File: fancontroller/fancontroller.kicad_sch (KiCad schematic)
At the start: 9 parts, among them SW1 SW_RESET, SW2 SW_BOOT, U1 ESP32-WROOM-32, U2 AMS1117-3.3

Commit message: KIcad messing
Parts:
- removed C1: 1uF, symbol Device:C
- removed C2, C4: 10uF, symbol Device:C
- removed C3: 0.1uF, symbol Device:C
- removed R1: 10k, symbol Device:R
- removed SW1: SW_RESET, symbol Switch:SW_Push
- removed SW2: SW_BOOT, symbol Switch:SW_Push
- removed U1: ESP32-WROOM-32, RF_Module:ESP32-WROOM-32, symbol RF_Module:ESP32-WROOM-32
- removed U2: AMS1117-3.3, Package_TO_SOT_SMD:SOT-223-3_TabPin2, symbol Regulator_Linear:AMS1117-3.3
- added C6: 10uF, Capacitor_THT:CP_Radial_D4.0mm_P1.50mm, symbol Device:C_Polarized
- added C7, C9: 0.1uF, Capacitor_THT:C_Disc_D3.0mm_W2.0mm_P2.50mm, symbol Device:C
- added C8: 100uF, Capacitor_THT:CP_Radial_D5.0mm_P2.00mm, symbol Device:C_Polarized
- added J2: Power Terminal, TerminalBlock:TerminalBlock_bornier-2_P5.08mm, symbol Connector:Screw_Terminal_01x02
- added J3: Programmer, Connector_PinHeader_2.54mm:PinHeader_1x04_P2.54mm_Vertical, symbol Connector:Conn_01x04_Male
- added J4: Relay board output, Connector_PinHeader_2.54mm:PinHeader_1x10_P2.54mm_Vertical, symbol Connector:Conn_01x10_Male
- added J5: I2C, Connector_PinHeader_2.54mm:PinHeader_1x04_P2.54mm_Vertical, symbol Connector:Conn_01x04_Male
- added R2, R3, R4, R5: 10k, Resistor_THT:R_Axial_DIN0207_L6.3mm_D2.5mm_P7.62mm_Horizontal, symbol Device:R
- added R6, R7, R8, R9: 470, Resistor_THT:R_Axial_DIN0207_L6.3mm_D2.5mm_P7.62mm_Horizontal, symbol Device:R
- added SW3: SW_Push, symbol Switch:SW_Push
- added U3: AMS1117-3.3, Package_TO_SOT_SMD:SOT-223-3_TabPin2, symbol Regulator_Linear:AMS1117-3.3
- added U4: ESP-12F, RF_Module:ESP-12E, symbol RF_Module:ESP-12F
- added U5: 74HC595, Package_DIP:DIP-16_W7.62mm_Socket, symbol 74xx:74HC595
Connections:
- net +3.3V: now also J3.1 (Pin_1)
- net GND: now also C6.2, C7.1, C8.2, C9.2, J2.2 (Pin_2), J3.4 (Pin_4), J4.1 (Pin_1), J5.4 (Pin_4), R5.1, SW3.1, U3.1 (GND), U4.15 (GND), U5.13 (~{OE}), U5.8 (GND)
- net RX: now also J3.2 (Pin_2), R7.2
- net TX: now also J3.3 (Pin_3), R6.1
- new net: J4.8 (Pin_8), U5.1 (QB)
- new net: J4.9 (Pin_9), U5.15 (QA)
- new net: J4.7 (Pin_7), U5.2 (QC)
- new net: J4.6 (Pin_6), U5.3 (QD)
- new net: J4.5 (Pin_5), U5.4 (QE)
- new net: J4.4 (Pin_4), U5.5 (QF)
- new net: J4.3 (Pin_3), U5.6 (QG)
- new net: J4.2 (Pin_2), U5.7 (QH)
- new net: R5.2, U4.16 (GPIO15)
- new net: R7.1, U4.21 (GPIO3/RXD)
- new net: R6.2, U4.22 (GPIO1/TXD)
- new net: C7.2, R4.1, U4.3 (EN)
- new net +3V3: C8.1, C9.1, J5.1 (Pin_1), R2.1, R3.1, R4.2, R8.1, R9.1, U3.2 (VO), U4.8 (VCC), U5.10 (~{SRCLR}), U5.16 (VCC)
- new net +5V: C6.1, J2.1 (Pin_1), J4.10 (Pin_10), U3.3 (VI)
- new net GPIO0: R2.2, SW3.2, U4.18 (GPIO0)
- new net MD_1: U4.6 (GPIO12), U5.12 (RCLK)
- new net MD_2: U4.7 (GPIO13), U5.11 (SRCLK)
- new net MD_3: U4.5 (GPIO14), U5.14 (SER)
- new net RST: R3.2, U4.1 (~{RST})
- new net SCL: J5.2 (Pin_2), R9.2, U4.20 (GPIO5)
- new net SDA: J5.3 (Pin_3), R8.2, U4.19 (GPIO4)
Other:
- note added: "Enabling booting"
- note added: "Output Multiplexer"
- note added: "Power circuit"

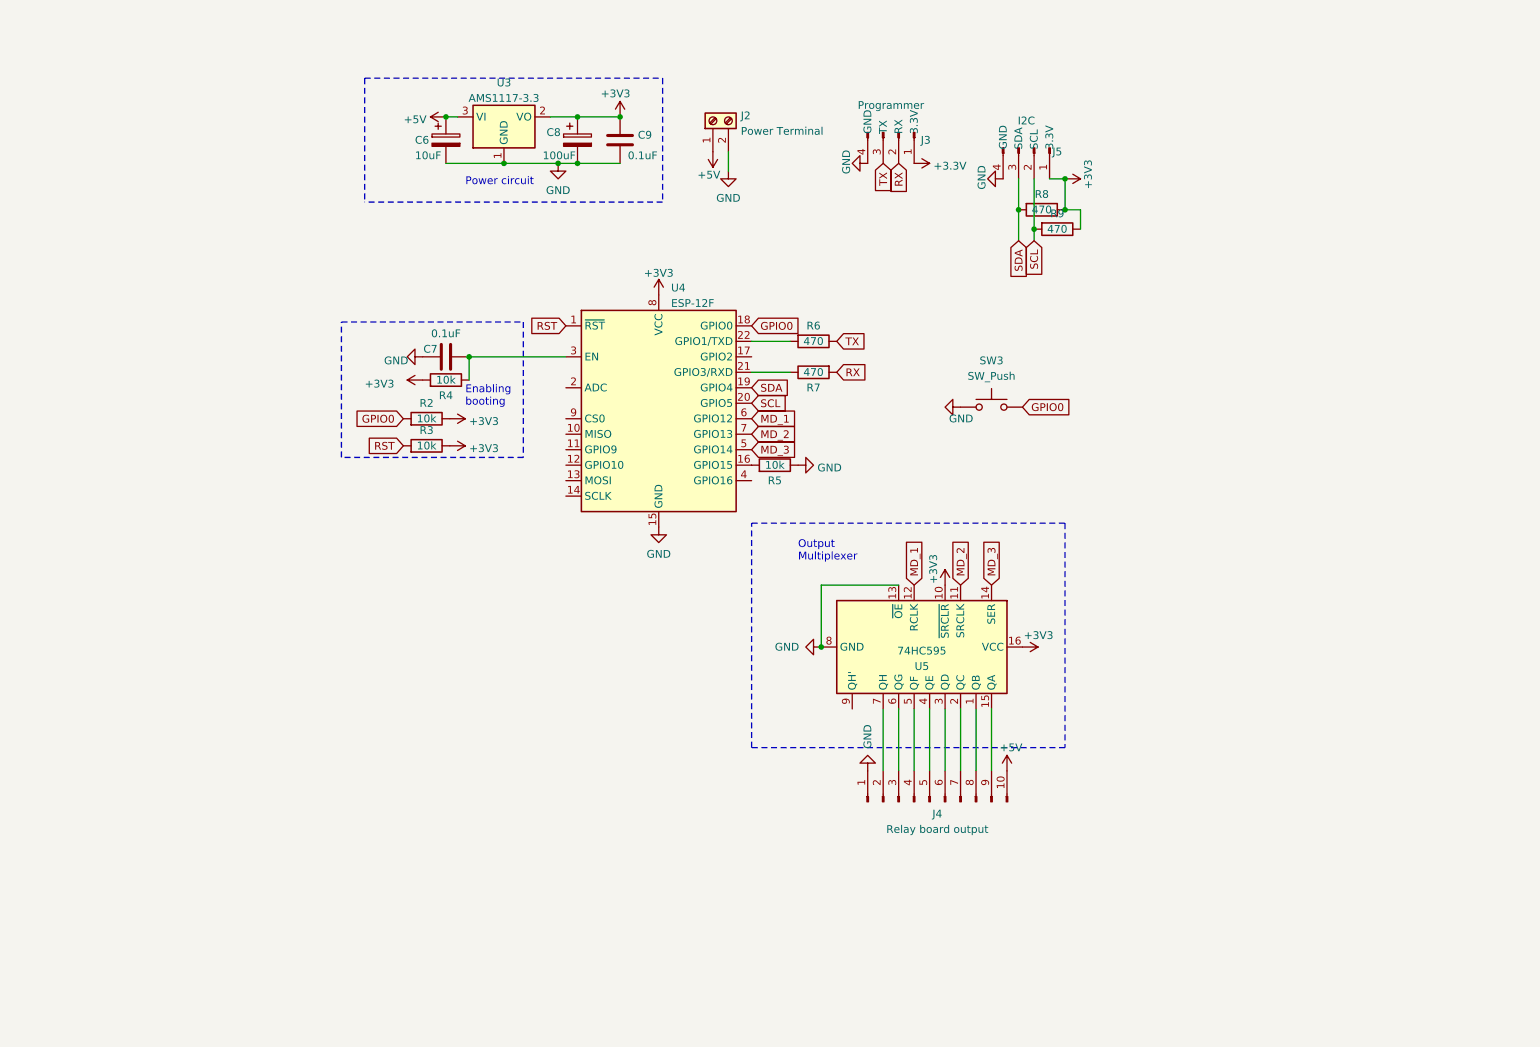
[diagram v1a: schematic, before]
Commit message: Auf esp32 festlegen und schematik anfangen
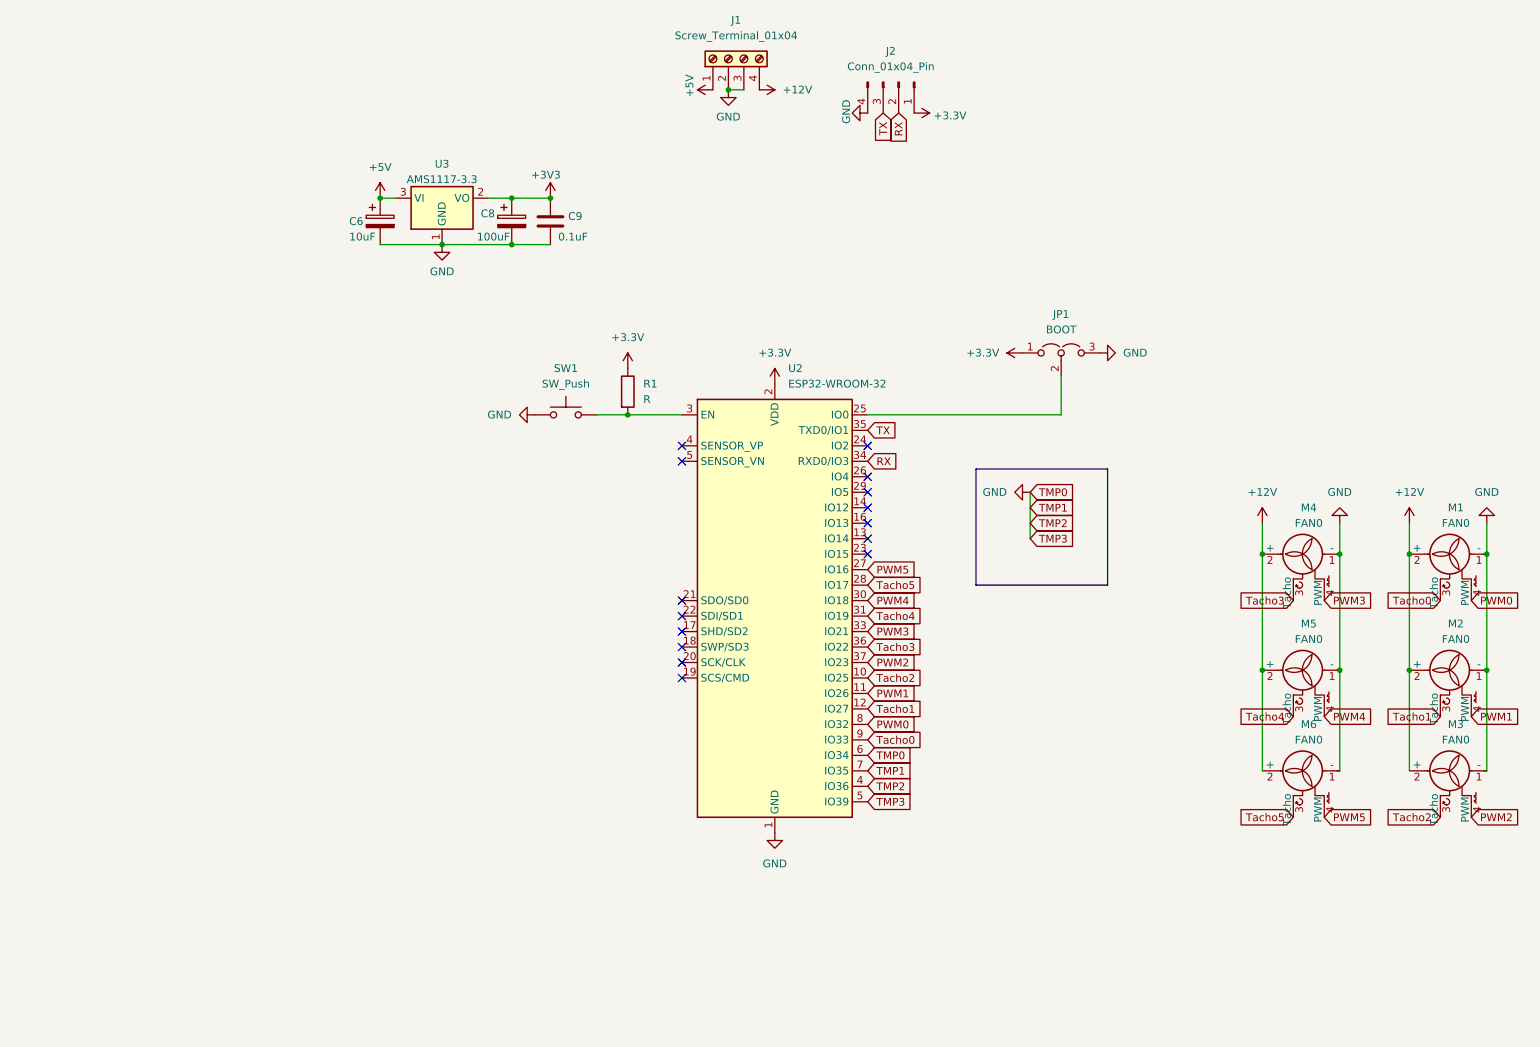
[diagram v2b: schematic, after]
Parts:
- removed C7: 0.1uF, Capacitor_THT:C_Disc_D3.0mm_W2.0mm_P2.50mm, symbol Device:C
- removed J2: Power Terminal, TerminalBlock:TerminalBlock_bornier-2_P5.08mm, symbol Connector:Screw_Terminal_01x02
- removed J3: Programmer, Connector_PinHeader_2.54mm:PinHeader_1x04_P2.54mm_Vertical, symbol Connector:Conn_01x04_Male
- removed J4: Relay board output, Connector_PinHeader_2.54mm:PinHeader_1x10_P2.54mm_Vertical, symbol Connector:Conn_01x10_Male
- removed J5: I2C, Connector_PinHeader_2.54mm:PinHeader_1x04_P2.54mm_Vertical, symbol Connector:Conn_01x04_Male
- removed R2, R3, R4, R5: 10k, Resistor_THT:R_Axial_DIN0207_L6.3mm_D2.5mm_P7.62mm_Horizontal, symbol Device:R
- removed R6, R7, R8, R9: 470, Resistor_THT:R_Axial_DIN0207_L6.3mm_D2.5mm_P7.62mm_Horizontal, symbol Device:R
- removed SW3: SW_Push, symbol Switch:SW_Push
- removed U4: ESP-12F, RF_Module:ESP-12E, symbol RF_Module:ESP-12F
- removed U5: 74HC595, Package_DIP:DIP-16_W7.62mm_Socket, symbol 74xx:74HC595
- added J1: Screw_Terminal_01x04, symbol Connector:Screw_Terminal_01x04
- added J2: Conn_01x04_Pin, symbol Connector:Conn_01x04_Pin
- added JP1: BOOT, symbol Jumper:Jumper_3_Open
- added M1, M2, M3, M4, M5, M6: FAN0, symbol Motor:Fan_Tacho_PWM
- added R1: R, symbol Device:R
- added SW1: SW_Push, symbol Switch:SW_Push
- added U2: ESP32-WROOM-32, RF_Module:ESP32-WROOM-32, symbol Custom:ESP32-WROOM-32
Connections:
- net +3.3V: now also J2.1 (Pin_1), JP1.1 (A), R1.1, U2.2 (VDD)
- net +5V: now also J1.1 (Pin_1)
- net GND: now also J1.2 (Pin_2), J1.3 (Pin_3), J2.4 (Pin_4), JP1.3 (B), M1.1 (-), M2.1 (-), M3.1 (-), M4.1 (-), M5.1 (-), M6.1 (-), SW1.1, U2.1 (GND), U2.4 (SENSOR_VP), U2.5 (SENSOR_VN), U2.6 (IO34), U2.7 (IO35)
- net RX: now also J2.2 (Pin_2), U2.34 (RXD0/IO3)
- net TX: now also J2.3 (Pin_3), U2.35 (TXD0/IO1)
- new net: R1.2, SW1.2, U2.3 (EN)
- new net: JP1.2 (C), U2.25 (IO0)
- new net: U2.15 (GND), U2.38 (GND), U2.39 (GND)
- new net +12V: J1.4 (Pin_4), M1.2 (+), M2.2 (+), M3.2 (+), M4.2 (+), M5.2 (+), M6.2 (+)
- new net PWM0: M1.4 (PWM), U2.8 (IO32)
- new net PWM1: M2.4 (PWM), U2.11 (IO26)
- new net PWM2: M3.4 (PWM), U2.37 (IO23)
- new net PWM3: M4.4 (PWM), U2.33 (IO21)
- new net PWM4: M5.4 (PWM), U2.30 (IO18)
- new net PWM5: M6.4 (PWM), U2.27 (IO16)
- new net Tacho0: M1.3 (Tacho), U2.9 (IO33)
- new net Tacho1: M2.3 (Tacho), U2.12 (IO27)
- new net Tacho2: M3.3 (Tacho), U2.10 (IO25)
- new net Tacho3: M4.3 (Tacho), U2.36 (IO22)
- new net Tacho4: M5.3 (Tacho), U2.31 (IO19)
- new net Tacho5: M6.3 (Tacho), U2.28 (IO17)
- no-connect marks 0 -> 15
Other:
- note removed: "Enabling booting"
- note removed: "Output Multiplexer"
- note removed: "Power circuit"
- moved on the sheet: C6, C8, C9, U3

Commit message: Massiver Fortschritt. Die Schematik scheint fertig zu sein und das tracing hat begonnen. Schritt für schritt werden Label von io vertauscht, um das tracen zu vereinfachen
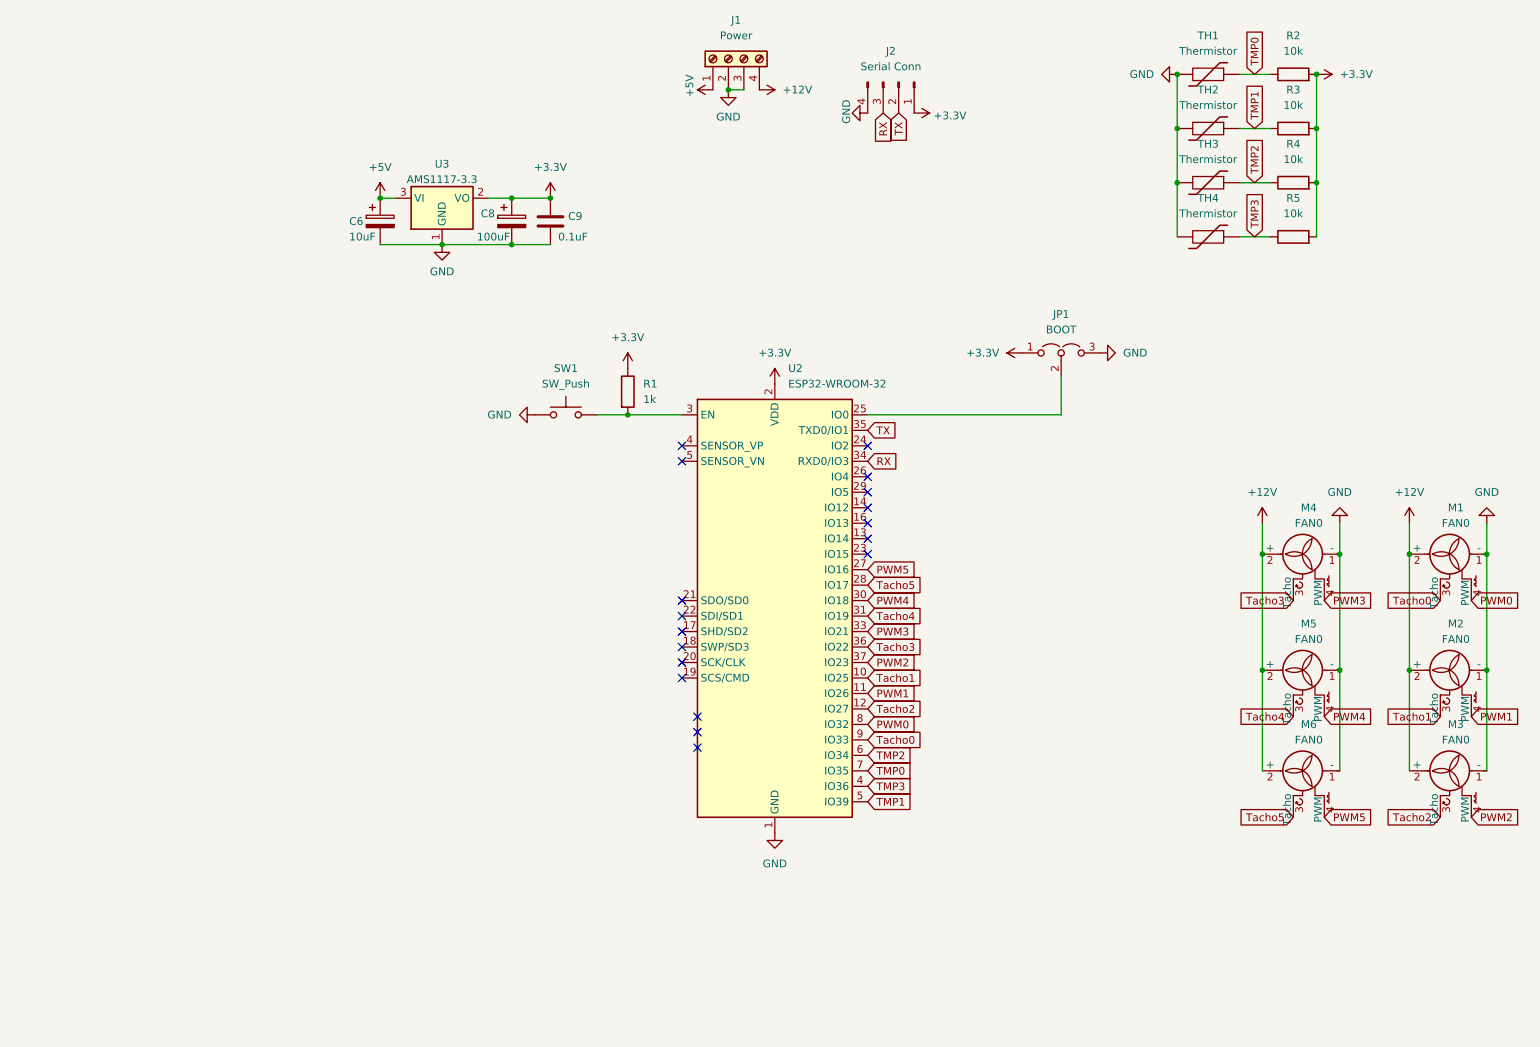
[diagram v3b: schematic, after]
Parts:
- added R2, R3, R4, R5: 10k, Resistor_SMD:R_0805_2012Metric, symbol Device:R
- added TH1, TH2, TH3, TH4: Thermistor, Connector_PinHeader_2.54mm:PinHeader_1x02_P2.54mm_Vertical, symbol Device:Thermistor
- J1: value Screw_Terminal_01x04 -> Power; footprint (none) -> Connector_PinHeader_2.54mm:PinHeader_1x04_P2.54mm_Horizontal
- J2: value Conn_01x04_Pin -> Serial Conn; footprint (none) -> Connector_PinHeader_2.54mm:PinHeader_1x04_P2.54mm_Horizontal
- JP1: footprint (none) -> Connector_PinHeader_2.54mm:PinHeader_1x03_P2.54mm_Vertical
- M1, M2, M3, M4, M5, M6: footprint (none) -> Connector:FanPinHeader_1x04_P2.54mm_Vertical
- R1: value R -> 1k; footprint (none) -> Resistor_SMD:R_0805_2012Metric
- SW1: footprint (none) -> Connector_PinHeader_2.54mm:PinHeader_1x02_P2.54mm_Vertical
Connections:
- net +3V3 is gone; now on net +3.3V: C8.1, C9.1, U3.2 (VO)
- net +3.3V: now also R2.2, R3.2, R4.2, R5.2
- net GND: now also TH1.2, TH2.2, TH3.2, TH4.2; no longer U2.4 (SENSOR_VP), U2.5 (SENSOR_VN), U2.6 (IO34), U2.7 (IO35)
- net RX: now also J2.3 (Pin_3); no longer J2.2 (Pin_2)
- net TX: now also J2.2 (Pin_2); no longer J2.3 (Pin_3)
- net Tacho1: now also U2.10 (IO25); no longer U2.12 (IO27)
- net Tacho2: now also U2.12 (IO27); no longer U2.10 (IO25)
- net TMP3: now reaches U2.4 (SENSOR_VP)
- net TMP3: now also R5.1, TH4.1
- net TMP1: now reaches U2.5 (SENSOR_VN)
- net TMP1: now also R3.1, TH2.1
- new net TMP0: R2.1, TH1.1, U2.7 (IO35)
- new net TMP2: R4.1, TH3.1, U2.6 (IO34)
- now unconnected: U2.15 (GND), U2.38 (GND), U2.39 (GND)
- no-connect marks 15 -> 18

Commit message: First pcb iteration done
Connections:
- net GND: now also U2.39 (GND)
- net TMP1: now also U2.6 (IO34); no longer U2.5 (SENSOR_VN)
- net TMP2: now also U2.5 (SENSOR_VN); no longer U2.6 (IO34)
- no-connect marks 18 -> 17
